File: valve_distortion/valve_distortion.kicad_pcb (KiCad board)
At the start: 2 copper layers, 105.3 x 200 mm, 41 parts, among them J1 INPUT, J2 OUTPUT, J3 Conn_01x10, SW1 SW_ENABLE, U1 ECC83, U2 TL072

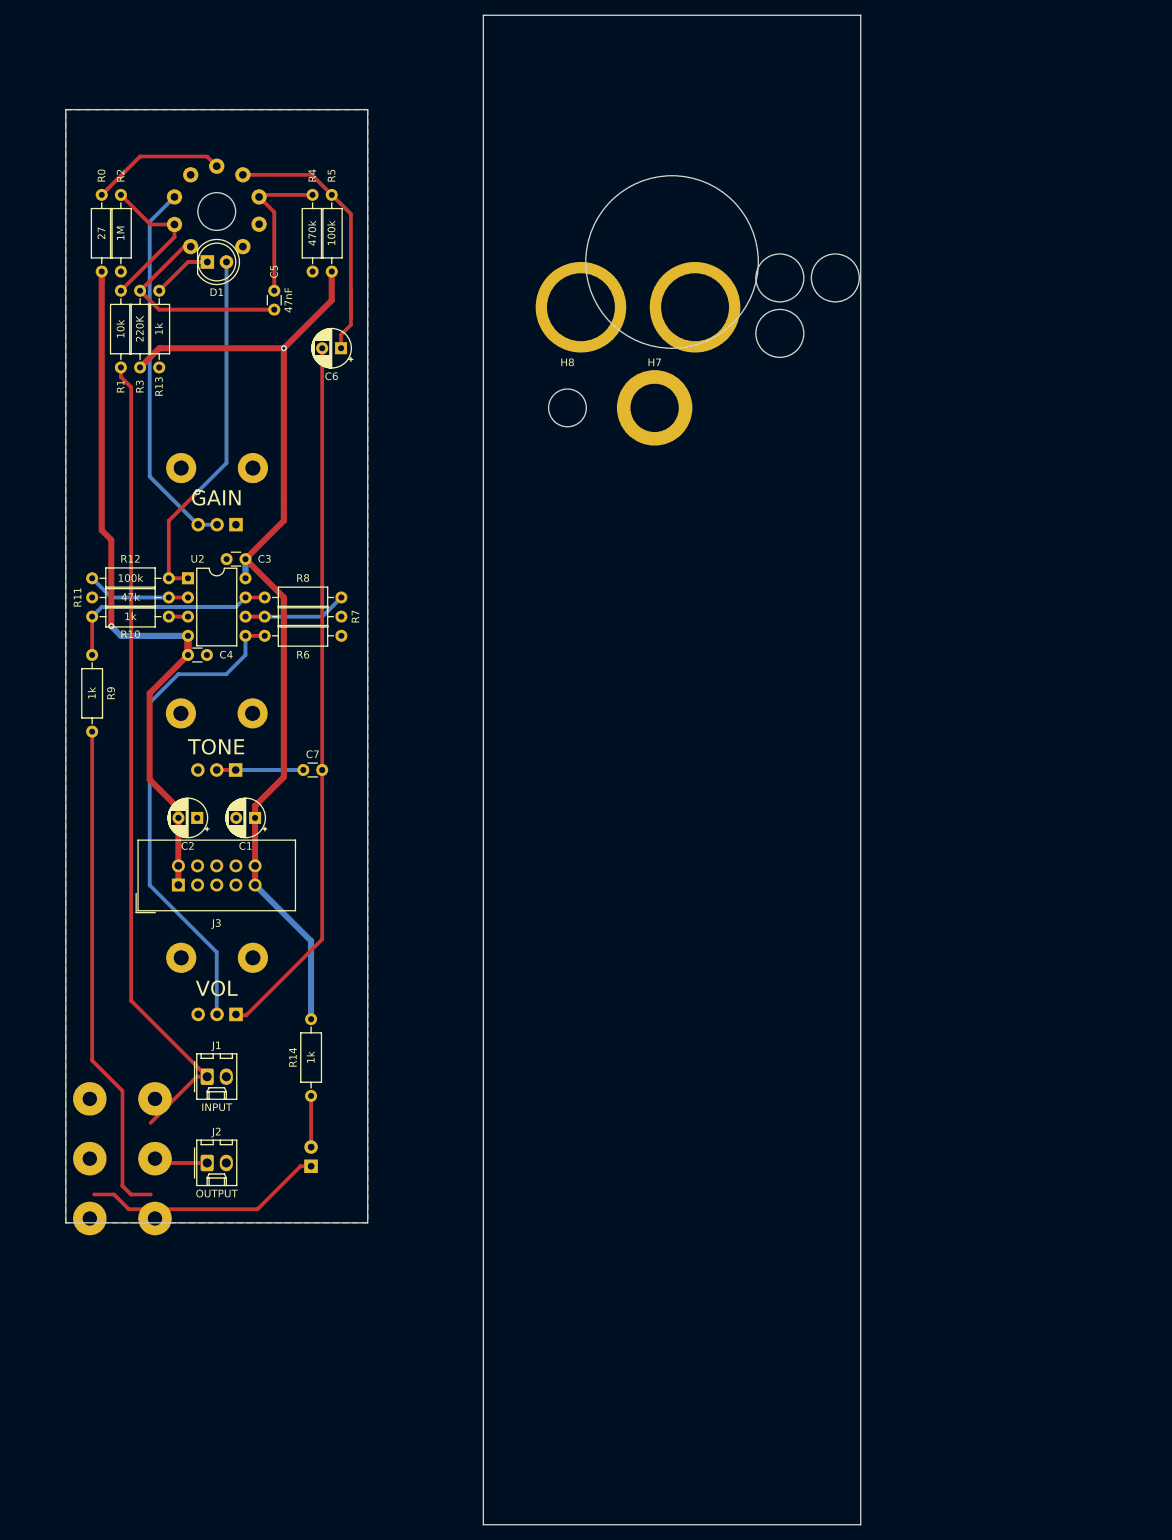
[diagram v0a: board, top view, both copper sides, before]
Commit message: Add complete files for valve distortion euro module
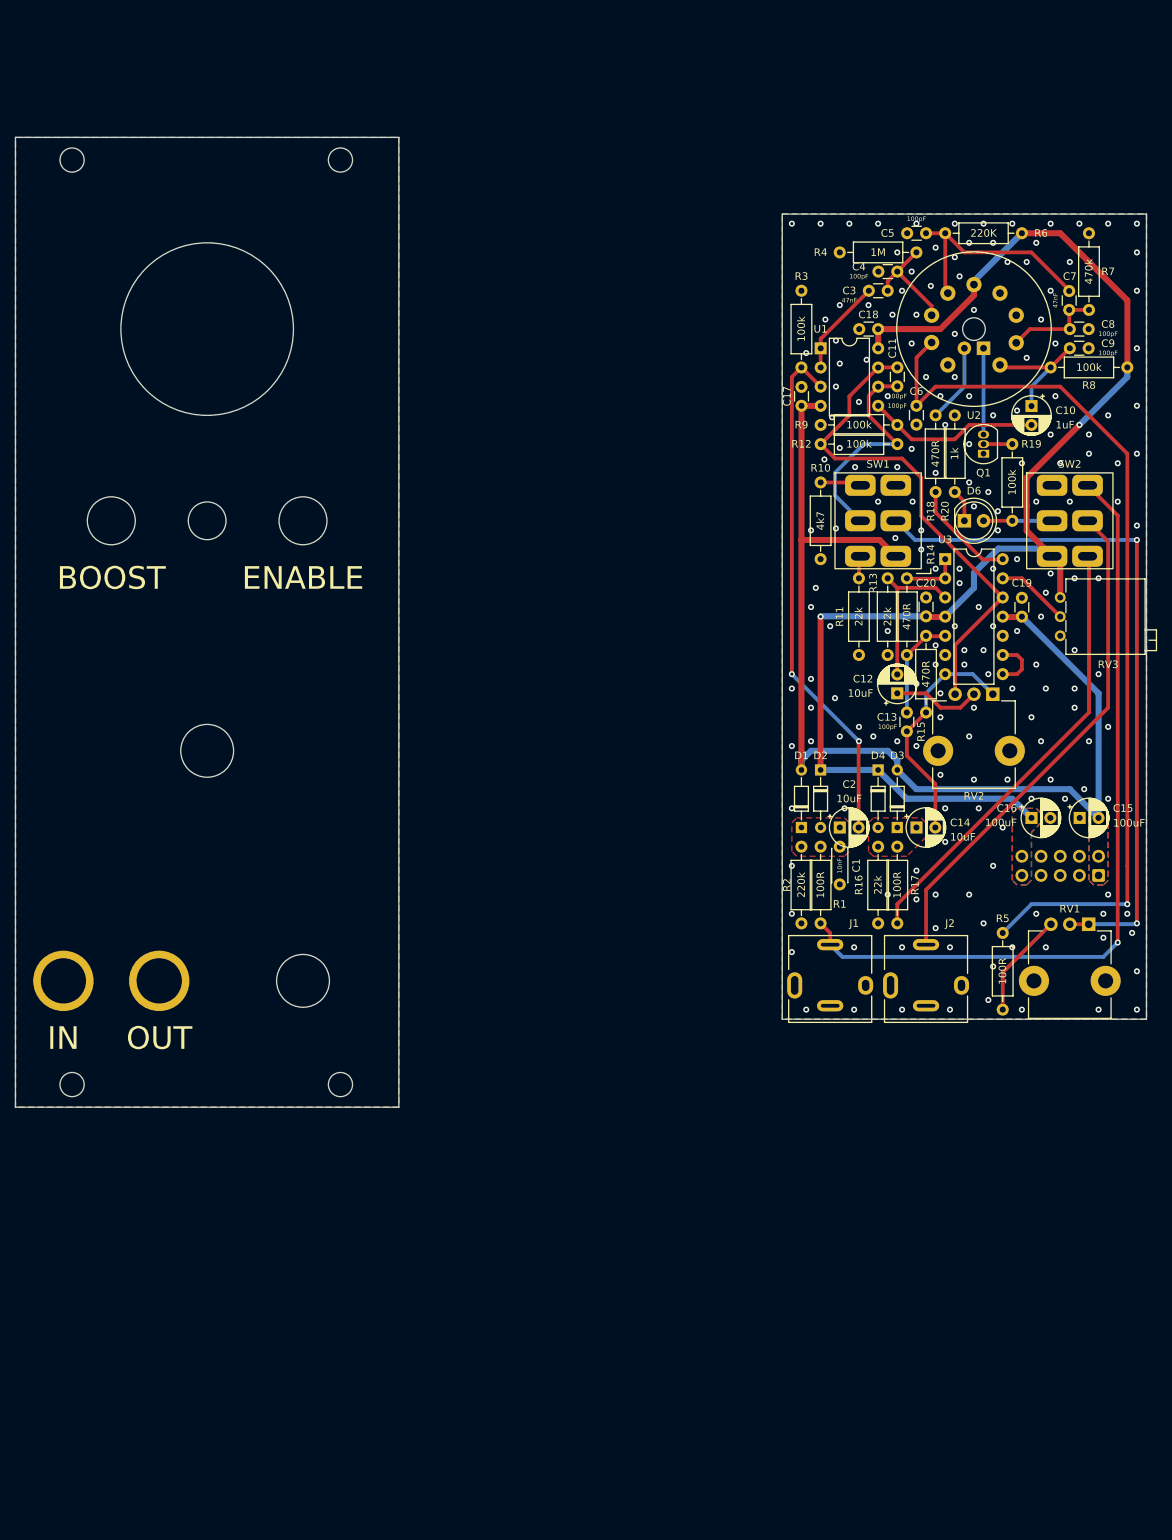
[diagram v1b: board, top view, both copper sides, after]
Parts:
- removed R0: 27, Resistor_THT:R_Axial_DIN0207_L6.3mm_D2.5mm_P10.16mm_Horizontal
- added C10: 1uF, Capacitor_THT:CP_Radial_D5.0mm_P2.50mm, F.Cu at (186.2, 74.3)
- added C11: 100pF, Capacitor_THT:C_Disc_D3.0mm_W1.6mm_P2.50mm, F.Cu at (168.4, 69.2)
- added C12: 10uF, Capacitor_THT:CP_Radial_D5.0mm_P2.50mm, F.Cu at (168.4, 112.3)
- added C13: 100pF, Capacitor_THT:C_Disc_D3.0mm_W1.6mm_P2.50mm, F.Cu at (169.7, 117.4)
- added C14: 10uF, Capacitor_THT:CP_Radial_D5.0mm_P2.50mm, F.Cu at (171.0, 130.1)
- added C15: 100uF, Capacitor_THT:CP_Radial_D5.0mm_P2.50mm, F.Cu at (192.6, 128.8)
- added C16: 100uF, Capacitor_THT:CP_Radial_D5.0mm_P2.50mm, F.Cu at (186.2, 128.8)
- added C17: 0.1uF, Capacitor_THT:C_Disc_D3.0mm_W1.6mm_P2.50mm, F.Cu at (155.7, 71.7)
- added C18: 0.1uF, Capacitor_THT:C_Disc_D3.0mm_W1.6mm_P2.50mm, F.Cu at (165.9, 64.1)
- added C19: 0.1uF, Capacitor_THT:C_Disc_D3.0mm_W1.6mm_P2.50mm, F.Cu at (184.9, 99.7)
- added C20: 0.1uF, Capacitor_THT:C_Disc_D3.0mm_W1.6mm_P2.50mm, F.Cu at (172.2, 102.1)
- added C8: 100pF, Capacitor_THT:C_Disc_D3.0mm_W1.6mm_P2.50mm, F.Cu at (191.3, 64.1)
- added C9: 100pF, Capacitor_THT:C_Disc_D3.0mm_W1.6mm_P2.50mm, F.Cu at (191.3, 66.6)
- added D3: 1N4148, Diode_THT:D_DO-34_SOD68_P7.62mm_Horizontal, F.Cu at (168.4, 130.1)
- added D4: 1N4148, Diode_THT:D_DO-34_SOD68_P7.62mm_Horizontal, F.Cu at (165.9, 122.5)
- added D5: NTE30033, LED_THT:LED_D3.0mm_Clear, B.Cu at (179.8, 66.6)
- added D6: ENABLE, LED_THT:LED_D5.0mm, F.Cu at (177.3, 89.5)
- added H10: Pot, kosmo-lib:Hole_Pot, F.Cu at (89.7, 150.4)
- added H11: Jack, kosmo-lib:Hole_Jack_3.5mm, F.Cu at (57.9, 150.4)
- added H12: Jack, kosmo-lib:Hole_Jack_3.5mm, F.Cu at (70.6, 150.4)
- added H9: Pot, kosmo-lib:Hole_Pot, F.Cu at (77.0, 120.0)
- added Q1: 2N3904, Package_TO_SOT_THT:TO-92_Inline, F.Cu at (179.8, 80.6)
- added R15: 470R, Resistor_THT:R_Axial_DIN0207_L6.3mm_D2.5mm_P10.16mm_Horizontal, F.Cu at (172.2, 104.7)
- added R16: 22k, Resistor_THT:R_Axial_DIN0207_L6.3mm_D2.5mm_P10.16mm_Horizontal, F.Cu at (165.9, 132.7)
- added R17: 100R, Resistor_THT:R_Axial_DIN0207_L6.3mm_D2.5mm_P10.16mm_Horizontal, F.Cu at (168.4, 132.7)
- added R18: 470R, Resistor_THT:R_Axial_DIN0207_L6.3mm_D2.5mm_P10.16mm_Horizontal, F.Cu at (173.5, 85.7)
- added R19: 100k, Resistor_THT:R_Axial_DIN0207_L6.3mm_D2.5mm_P10.16mm_Horizontal, F.Cu at (183.7, 79.3)
- added R20: 1k, Resistor_THT:R_Axial_DIN0207_L6.3mm_D2.5mm_P10.16mm_Horizontal, F.Cu at (176.0, 85.7)
- added SW2: ENABLE, kosmo-lib:Switch_DPDT, F.Cu at (191.3, 89.5)
- added U3: TL074, Package_DIP:DIP-14_W7.62mm, F.Cu at (174.8, 94.6)
- C1: value 10uF -> 10nF; footprint Capacitor_THT:CP_Radial_D5.0mm_P2.50mm -> Capacitor_THT:C_Disc_D4.3mm_W1.9mm_P5.00mm
- C3: value 0.1uF -> 47nF
- C4: value 0.1uF -> 100pF
- C5: value 47nF -> 100pF
- C6: value 1uF -> 100pF; footprint Capacitor_THT:CP_Radial_D5.0mm_P2.50mm -> Capacitor_THT:C_Disc_D3.0mm_W1.6mm_P2.50mm
- C7: value 10nF -> 47nF
- D1: value LED_SIG -> 1N4148; footprint LED_THT:LED_D5.0mm -> Diode_THT:D_DO-34_SOD68_P7.62mm_Horizontal
- D2: value LED_EN -> 1N4148; footprint LED_THT:LED_D5.0mm -> Diode_THT:D_DO-34_SOD68_P7.62mm_Horizontal; moved to F.Cu
- H1: value LED -> LED 3mm; footprint kosmo-lib:Hole_LED_5mm -> kosmo-lib:Hole_LED_3mm
- H2, H3, H4: value Pot -> 3.2mm Mounting Hole; footprint kosmo-lib:Hole_Pot -> MountingHole:MountingHole_3.2mm_M3
- H5: value Jack -> 3.2mm Mounting Hole; footprint kosmo-lib:Hole_Jack -> MountingHole:MountingHole_3.2mm_M3
- H6: value Jack -> Switch; footprint kosmo-lib:Hole_Jack -> kosmo-lib:Hole_Toggle_Switch
- H7: footprint MountingHole:MountingHole_6.4mm_M6_ISO14580_Pad -> kosmo-lib:Hole_Toggle_Switch
- H8: value LED -> LED 5mm; footprint MountingHole:MountingHole_5mm -> kosmo-lib:Hole_LED_5mm
- J1, J2: footprint Connector_Molex:Molex_KK-254_AE-6410-02A_1x02_P2.54mm_Vertical -> kosmo-lib:Jack_3.5mm_QingPu_WQP-PJ301BM
- J3: value Conn_01x10 -> Euro Power; moved to B.Cu
- R1: value 10k -> 100R
- R10: value 1k -> 4k7
- R11: value 47k -> 22k
- R13: value 1k -> 22k
- R14: value 1k -> 470R
- R2: value 1M -> 220k
- R3: value 220K -> 100k
- R4: value 470k -> 1M
- R5: value 100k -> 100R
- R6: value 10k -> 220K
- R7: value 470 -> 470k
- R8: value 10k -> 100k
- R9: value 1k -> 100k
- RV1, RV2: value 100k -> 100k LIN; moved to F.Cu
- RV3: value 100k -> 200k; footprint Potentiometer_THT:Potentiometer_TT_P0915N -> kosmo-lib:Potentiometer_Trim_Horizontal; moved to F.Cu
- SW1: value SW_ENABLE -> BOOST; footprint kosmo-lib:GR5-326-XXXX -> kosmo-lib:Switch_DPDT; moved to F.Cu
- U1: value ECC83 -> NE5532; footprint Valve:Valve_ECC-83-1 -> Package_DIP:DIP-8_W7.62mm; moved to F.Cu
- U2: value TL072 -> 12AX7; footprint Package_DIP:DIP-8_W7.62mm -> Valve:Valve_ECC-83-1
- moved H2 147.1 mm to (59.1, 164.2)
- moved SW1 131.0 mm to (165.9, 89.5)
- moved R1 125.0 mm to (158.3, 142.8), turned to 90 degrees
- moved R2 124.9 mm to (155.7, 132.7)
- moved R5 124.8 mm to (182.4, 144.1), turned to -90 degrees
- moved RV1 124.8 mm to (193.8, 142.9)
- moved J3 121.9 mm to (195.1, 136.5)
- moved RV3 121.3 mm to (190.0, 102.2)
- moved C7 118.4 mm to (191.2, 61.5), turned to 90 degrees
- moved R8 118.3 mm to (198.9, 69.2), turned to 180 degrees
- moved R7 116.5 mm to (193.8, 61.5), turned to 90 degrees
- moved R9 114.2 mm to (168.4, 76.8), turned to 180 degrees
- moved R6 113.6 mm to (184.9, 51.4), turned to 180 degrees
- moved U2 111.2 mm to (182.0, 68.8)
- moved D1 108.7 mm to (155.7, 130.1), turned to 90 degrees
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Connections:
- C1 pad 1: +12V -> /IN_FILTER
- C2 pad 1: GND -> /IN_FILTER
- C2 pad 2: -12V -> /IN_BUF_IN
- C3 pad 1: +12V -> /G1
- C3 pad 2: GND -> /DIST_IN
- C4 pad 1: GND -> /G1
- C4 pad 2: -12V -> GND
- C5 pad 1: Net-(C5-Pad1) -> /A1
- C5 pad 2: Net-(C5-Pad2) -> GND
- C6 pad 1: Net-(C6-Pad1) -> /K1
- C6 pad 2: Net-(C6-Pad2) -> GND
- C7 pad 1: Net-(C7-Pad1) -> /G2
- C7 pad 2: Net-(C6-Pad2) -> /A1
- D1 pad 1: Net-(D1-Pad1) -> /IN_FILTER
- D1 pad 2: Net-(D1-Pad2) -> -12V
- D2 pad 1: Net-(D2-Pad1) -> +12V
- D2 pad 2: Net-(D2-Pad2) -> /IN_FILTER
- J2 pad T: Net-(J2-PadT) -> /OUTPUT
- R1 pad 1: Net-(R1-Pad1) -> /INPUT
- R1 pad 2: /INPUT -> /IN_FILTER
- R10 pad 1: Net-(R10-Pad1) -> /BOOST_LOW
- R10 pad 2: Net-(R10-Pad2) -> GND
- R11 pad 1: Net-(R11-Pad1) -> /BOOST_HIGH
- R12 pad 1: Net-(D1-Pad2) -> /DIST_BUF_FB
- R12 pad 2: Net-(R11-Pad1) -> /DIST_OUT
- R13 pad 1: Net-(D1-Pad1) -> /VOL_BUF_IN
- R14 pad 1: Net-(D2-Pad2) -> /VOL_BUF_OUT
- R14 pad 2: +12V -> /VOL_INV_IN
- R2 pad 1: Net-(R1-Pad1) -> /IN_FILTER
- R3 pad 1: +12V -> /IN_BUF_IN
- R3 pad 2: Net-(C5-Pad2) -> GND
- R4 pad 1: Net-(C5-Pad1) -> /G1
- R5 pad 1: +12V -> /K1
- R5 pad 2: Net-(C6-Pad1) -> /GAIN
- R6 pad 1: Net-(R6-Pad1) -> +12V
- R6 pad 2: GND -> /A1
- R7 pad 1: Net-(R7-Pad1) -> /G2
- R8 pad 1: Net-(R10-Pad2) -> +12V
- R8 pad 2: Net-(R7-Pad1) -> /A2
- R9 pad 1: Net-(R9-Pad1) -> /DIST_BUF_IN
- R9 pad 2: Net-(R10-Pad2) -> GND
- RV1 pad 1: GND -> /K1_VOLTAGE
- RV1 pad 2: Net-(U1-Pad3) -> /K1_VOLTAGE
- RV1 pad 3: Net-(U1-Pad3) -> /GAIN
- RV2 pad 1: GND -> /VOL_OUT
- RV2 pad 2: Net-(C7-Pad1) -> /VOL_IN
- RV2 pad 3: Net-(C7-Pad1) -> /DIST_OUT
- RV3 pad 2: Net-(R6-Pad1) -> /LED_REF
- RV3 pad 3: Net-(C6-Pad2) -> +12V
- SW1 pad 1: Net-(D2-Pad1) -> /BOOST_LOW
- SW1 pad 2: GND -> /DIST_BUF_FB
- SW1 pad 3: unconnected-(SW1-Pad3) -> /BOOST_HIGH
- SW1 pad 4: Net-(R9-Pad1) -> GND
- SW1 pad 5: Net-(J2-PadT) -> /K1_VOLTAGE
- SW1 pad 6: /INPUT -> -12V
- U1 pad 1: Net-(C5-Pad2) -> /DIST_IN
- U1 pad 2: Net-(R1-Pad1) -> /DIST_IN
- U1 pad 3: Net-(U1-Pad3) -> /IN_BUF_IN
- U1 pad 4: GND -> -12V
- U1 pad 5: Net-(R0-Pad1) -> /DIST_BUF_IN
- U1 pad 6: Net-(C6-Pad1) -> /DIST_BUF_FB
- U1 pad 7: Net-(C5-Pad1) -> /DIST_OUT
- U1 pad 8: GND -> +12V
- U2 pad 1: Net-(D1-Pad2) -> /A2
- U2 pad 2: Net-(R11-Pad1) -> /G2
- U2 pad 3: Net-(R10-Pad1) -> GND
- U2 pad 4: -12V -> GND
- U2 pad 5: Net-(R6-Pad1) -> +12V
- U2 pad 6: Net-(R7-Pad1) -> /A1
- U2 pad 7: Net-(R10-Pad2) -> /G1
- U2 pad 8: +12V -> /K1
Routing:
- net /K1: track 0.00 -> 119.7 mm, vias 0 -> 1
- net Net-(C6-Pad2): track 94.0 -> 0.00 mm
- net /K1_VOLTAGE: track 0.00 -> 92.7 mm, vias 0 -> 2
- net /IN_BUF_IN: track 0.00 -> 68.8 mm, vias 0 -> 2
- net /OUTPUT: track 0.00 -> 67.3 mm
- net /DIST_OUT: track 0.00 -> 66.8 mm
- net Net-(R9-Pad1): track 66.1 -> 0.00 mm
- net Net-(R6-Pad1): track 65.5 -> 0.00 mm
- net /OUT_SW: track 0.00 -> 59.2 mm
- net Net-(U1-Pad3): track 49.9 -> 0.00 mm
- net -12V: track 94.9 -> 143.2 mm, vias 1 -> 0
- net Net-(D1-Pad2): track 47.6 -> 0.00 mm, vias 1 -> 0
- net +12V: track 133.2 -> 179.3 mm, vias 1 -> 2
- net Net-(C6-Pad1): track 38.3 -> 0.00 mm
- net Net-(D2-Pad1): track 31.9 -> 0.00 mm
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- added copper zone on B.Cu, net (none)
- added copper zone on F.Cu, net (none)
- added copper zone on B.Cu, net +12V
- added copper zone on F.Cu, net +12V
- added copper zone on B.Cu, net -12V
- added copper zone on F.Cu, net -12V
- added copper zone on F.Cu, net /IN_FILTER
- added copper zone on F.Cu, net /OUT_FILTER
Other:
- board size 105.3 x 200 mm -> 149.9 x 128.5 mm
- board text added: "BOOST"
- board text added: "ENABLE"
- board text added: "IN"
- board text added: "JLCJLCJLCJLC"
- board text added: "OUT"
- board text added: "VALVE DISTORTION"
- board text added: "Valve Distortion Max Proskauer v0.1 Jan 2023 https://github.com/mprosk/valve_distortion"
- board text added: "xperseai labs"
- board text removed: "GAIN"
- board text removed: "TONE"
- board text removed: "VOL"

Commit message: Fix rev1 pcb issues
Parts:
- moved R5 33.6 mm to (198.9, 114.9), turned to 180 degrees
- moved RV1 33.0 mm to (181.1, 112.5)
- moved RV2 33.0 mm to (193.8, 142.9)
- moved C19 5.00 mm to (184.9, 104.7), turned to 90 degrees
- moved C15 1.27 mm to (191.3, 128.8)
- moved J3 1.27 mm to (193.8, 136.5)
- moved C16 1.27 mm to (184.9, 128.8)
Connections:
- J1 pad TN: unconnected-(J1-PadTN) -> GND
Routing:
- net /K1: track 119.7 -> 76.2 mm, vias 1 -> 0
- net /DIST_OUT: track 66.8 -> 108.0 mm, vias 0 -> 1
- net /VOL_IN: track 11.7 -> 45.5 mm
- net /VOL_OUT: track 31.4 -> 57.1 mm
- net /OUT_SW: track 59.2 -> 81.2 mm
- net /K1_VOLTAGE: track 92.7 -> 75.0 mm
- net /OUTPUT: track 67.3 -> 84.8 mm
- net /INPUT: track 105.1 -> 108.1 mm, vias 1 -> 0
- net -12V: track 143.2 -> 141.4 mm
- net +12V: track 179.3 -> 178.0 mm
- net GND: vias 186 -> 199
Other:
- board text added: "Valve Distortion Max Proskauer v0.2 Feb 2023 https://github.com/mprosk/valve_distortion"
- board text removed: "Valve Distortion Max Proskauer v0.1 Jan 2023 https://github.com/mprosk/valve_distortion"
